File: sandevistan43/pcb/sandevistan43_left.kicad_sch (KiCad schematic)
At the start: 48 parts, among them J1 TRRS, SW1 SW_PUSH, SW10 SW_PUSH, SW11 SW_PUSH, SW12 SW_PUSH, SW13 SW_PUSH, SW14 SW_PUSH, SW15 SW_PUSH, SW16 SW_PUSH, SW17 SW_PUSH, SW18 SW_PUSH, SW19 SW_PUSH, SW2 SW_PUSH, SW20 SW_PUSH, SW21 SW_PUSH, SW22 SW_PUSH, SW3 SW_PUSH, SW4 SW_PUSH, SW5 SW_PUSH, SW6 SW_PUSH, SW7 SW_PUSH, SW8 SW_PUSH, SW9 SW_PUSH, U1 Pico

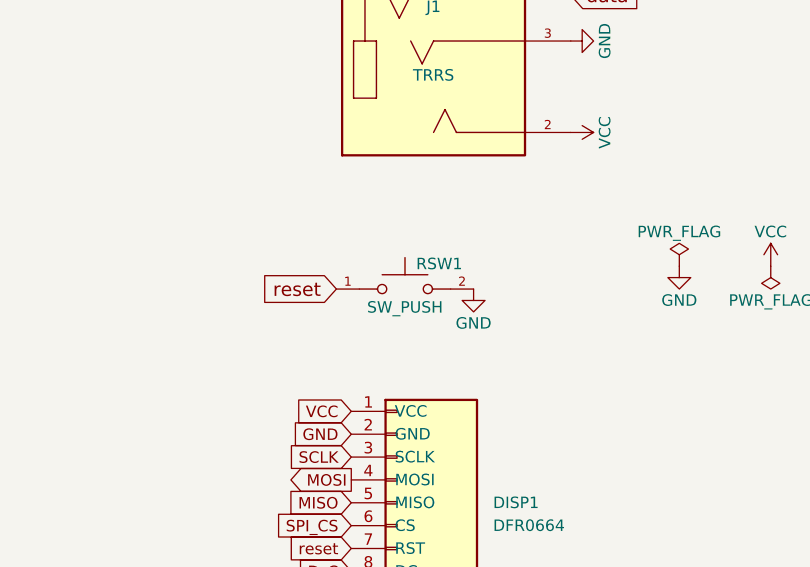
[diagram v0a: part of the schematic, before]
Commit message: Make footprints/symbols common and use easier to solder reset button
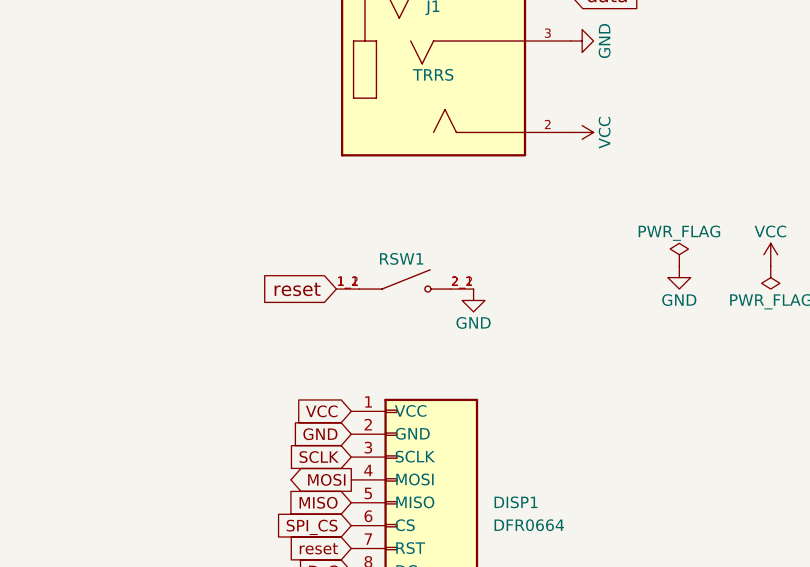
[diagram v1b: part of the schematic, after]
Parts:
- DISP1: symbol sandevistan43:DFR0664 -> isla-kbd:DFR0664
- RSW1: footprint TL6340AF160Q:SW_TL6340AF160Q -> EVQ-P7C01P:SW_EVQ-P7C01P; symbol TL6340AF160Q:TL6340AF160Q -> EVQ-P7C01P:EVQ-P7C01P; Availability (none) -> In Stock; Check_prices (none) -> https://www.snapeda.com/parts/EVQP7C01P/Panasonic/view-part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; Description_1 (none) -> TACTILE SW, SPST-NO, 0.05A, 12V, SMD; Product Range:EVQP7 S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; MANUFACTURER E-Swtich -> Panasonic Electronic Components; MAXIMUM_PACKAGE_HEIGHT 1.55mm -> 1.35mm; MF (none) -> Panasonic; MP (none) -> EVQP7C01P; PARTREV 10.23.2019 -> 2022.4; Package (none) -> None; Price (none) -> None; SnapEDA_Link (none) -> https://www.snapeda.com/parts/EVQP7C01P/Panasonic/view-part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
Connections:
- net GND: now also RSW1.2_1, RSW1.2_2; no longer RSW1.2
- net reset: now also RSW1.1_1, RSW1.1_2; no longer RSW1.1
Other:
- moved on the sheet: RSW1
